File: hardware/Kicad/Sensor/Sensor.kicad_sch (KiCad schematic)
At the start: 9 parts

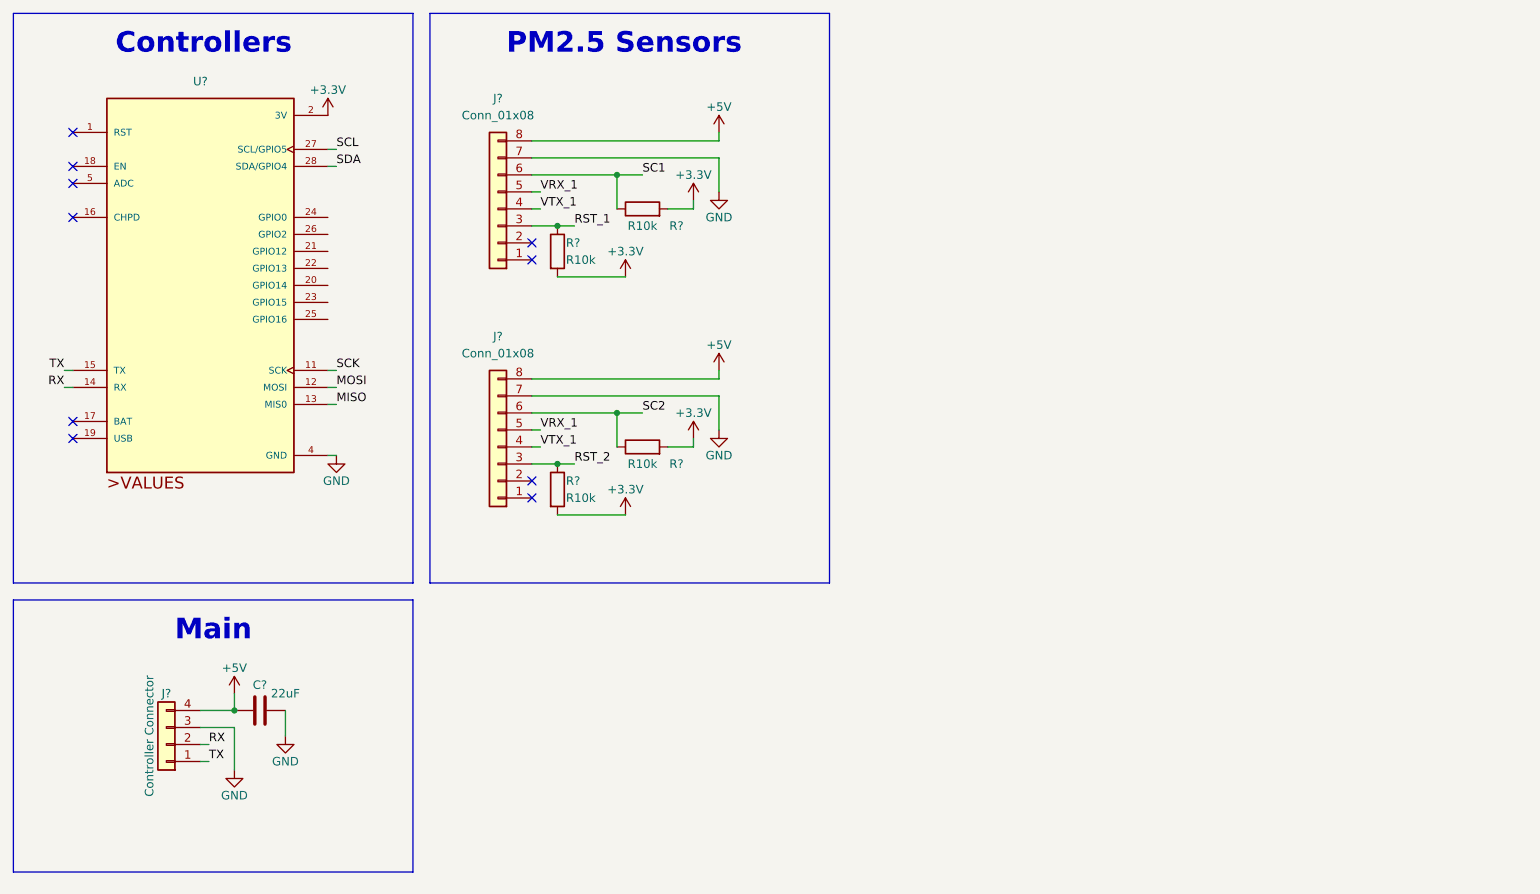
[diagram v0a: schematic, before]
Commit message: finished sensor PCB
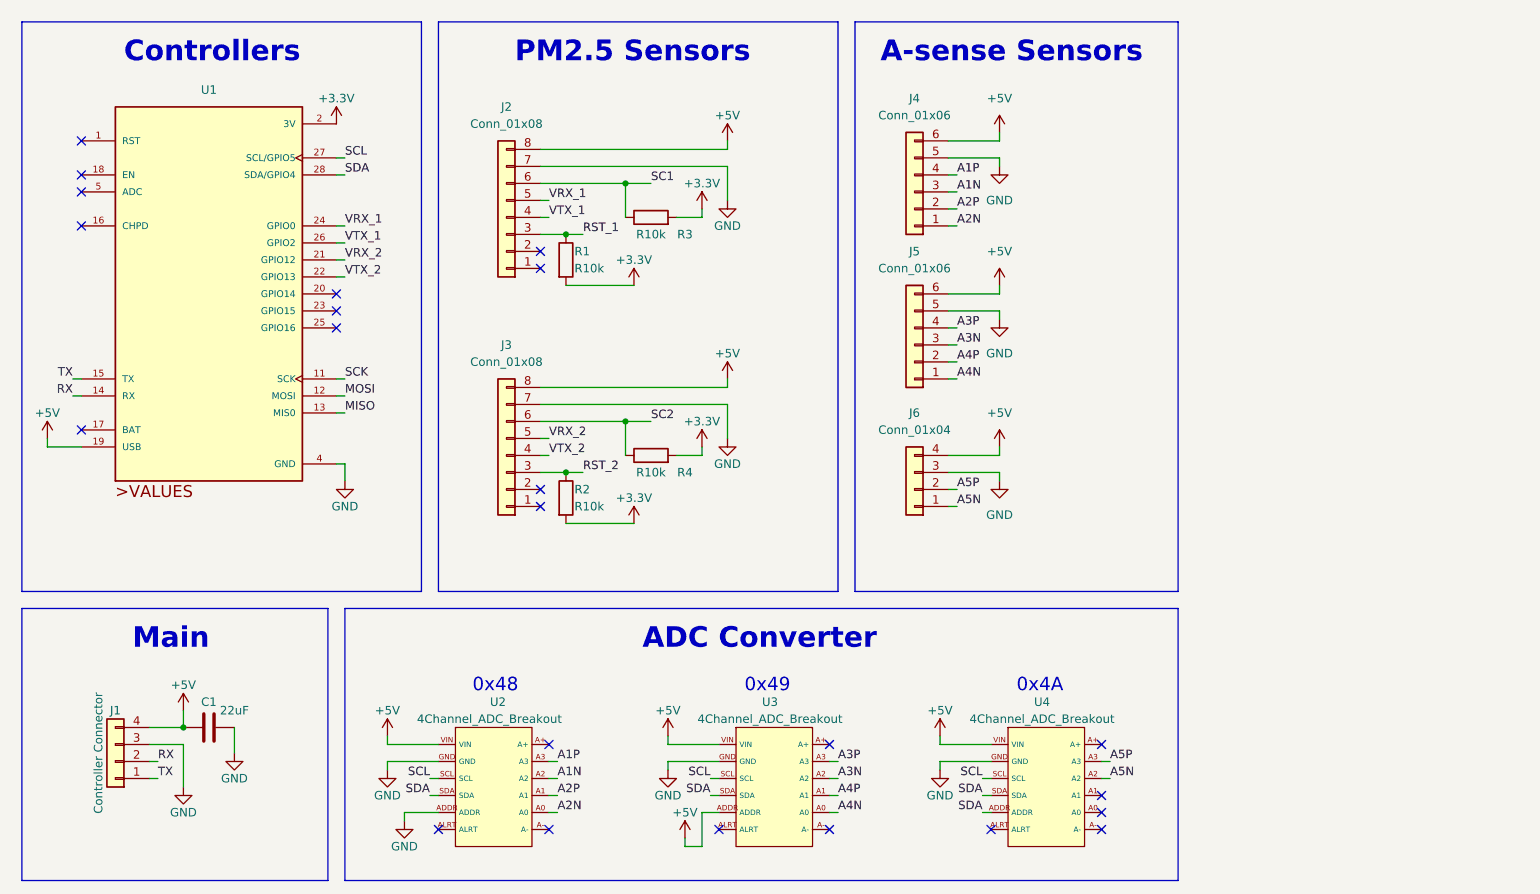
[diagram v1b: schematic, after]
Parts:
- added J4, J5: Conn_01x06, JST:JST_XH_B06B-XH-A_06x2.50mm_Straight, symbol Connector_Generic:Conn_01x06
- added J6: Conn_01x04, JST:JST_XH_B04B-XH-A_04x2.50mm_Straight, symbol Connector_Generic:Conn_01x04
- added U2, U3, U4: 4Channel_ADC_Breakout, Adafruit_Sensors:4Channel ADC Breakout, symbol Adafruit_Files:4Channel_ADC_Breakout
- J2, J3: renamed from J?; footprint (none) -> Connector_Molex:Molex_CLIK-Mate_502386-0870_1x08-1MP_P1.25mm_Horizontal
- R1, R2, R3, R4: renamed from R?; footprint (none) -> Resistor_SMD:R_1206_3216Metric
- gave numbers to parts that had none: 3
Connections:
- net +5V: now also U1.19 (USB), J4.6 (Pin_6), J5.6 (Pin_6), J6.4 (Pin_4), U2.VIN, U3.ADDR, U3.VIN, U4.VIN
- net GND: now also J4.5 (Pin_5), J5.5 (Pin_5), J6.3 (Pin_3), U2.ADDR, U2.GND, U3.GND, U4.GND
- net SCL: now also U2.SCL, U3.SCL, U4.SCL
- net SDA: now also U2.SDA, U3.SDA, U4.ADDR, U4.SDA
- net VRX_1: now also U1.24 (GPIO0); no longer J3.5 (Pin_5)
- net VTX_1: now also U1.26 (GPIO2); no longer J3.4 (Pin_4)
- net VRX_2: now reaches U1.21 (GPIO12)
- net VRX_2: now also J3.5 (Pin_5)
- net VTX_2: now reaches U1.22 (GPIO13)
- net VTX_2: now also J3.4 (Pin_4)
- new net A1N: J4.3 (Pin_3), U2.A2
- new net A1P: J4.4 (Pin_4), U2.A3
- new net A2N: J4.1 (Pin_1), U2.A0
- new net A2P: J4.2 (Pin_2), U2.A1
- new net A3N: J5.3 (Pin_3), U3.A2
- new net A3P: J5.4 (Pin_4), U3.A3
- new net A4N: J5.1 (Pin_1), U3.A0
- new net A4P: J5.2 (Pin_2), U3.A1
- new net A5N: J6.1 (Pin_1), U4.A2
- new net A5P: J6.2 (Pin_2), U4.A3
- no-connect marks 10 -> 23
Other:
- note added: "0x48"
- note added: "0x49"
- note added: "0x4A"
- note added: "A-sense Sensors"
- note added: "ADC Converter"
- moved on the sheet: C1, J1, J2, J3, R1, R2, R3, R4, U1

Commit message: updated PCBS
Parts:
- removed U4: 4Channel_ADC_Breakout, Adafruit_Sensors:4Channel ADC Breakout, symbol Adafruit_Files:4Channel_ADC_Breakout
- added U4: MicroSD_Breakout, Adafruit_Sensors:MicroSD_Breakout, symbol Adafruit_Files:MicroSD_Breakout
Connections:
- net A5N is gone; now on net A3P: J6.1 (Pin_1)
- net A5P is gone; now on net A3N: J6.2 (Pin_2)
- net +5V: now also U4.5V
- net A1N: now also J4.2 (Pin_2); no longer J4.3 (Pin_3)
- net A2N: now also J5.2 (Pin_2); no longer J4.1 (Pin_1)
- net A2P: now also J5.4 (Pin_4); no longer J4.2 (Pin_2)
- net A3N: no longer J5.3 (Pin_3)
- net A3P: no longer J5.4 (Pin_4)
- net GND: now also J4.1 (Pin_1), J4.3 (Pin_3), J5.1 (Pin_1), J5.3 (Pin_3), U4.GND
- net MISO: now also U4.DO
- net MOSI: now also U4.DI
- net SCK: now also U4.CLK
- net CS1: now reaches U1.20 (GPIO14)
- net CS1: now also U4.CS
- net A4N: no longer names the net of U3.A0
- net A4N: no longer J5.1 (Pin_1)
- net A4P: no longer names the net of U3.A1
- net A4P: no longer J5.2 (Pin_2)
- no-connect marks 23 -> 20
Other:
- note added: "Micro SD"
- note removed: "0x4A"
- moved on the sheet: J5, J6

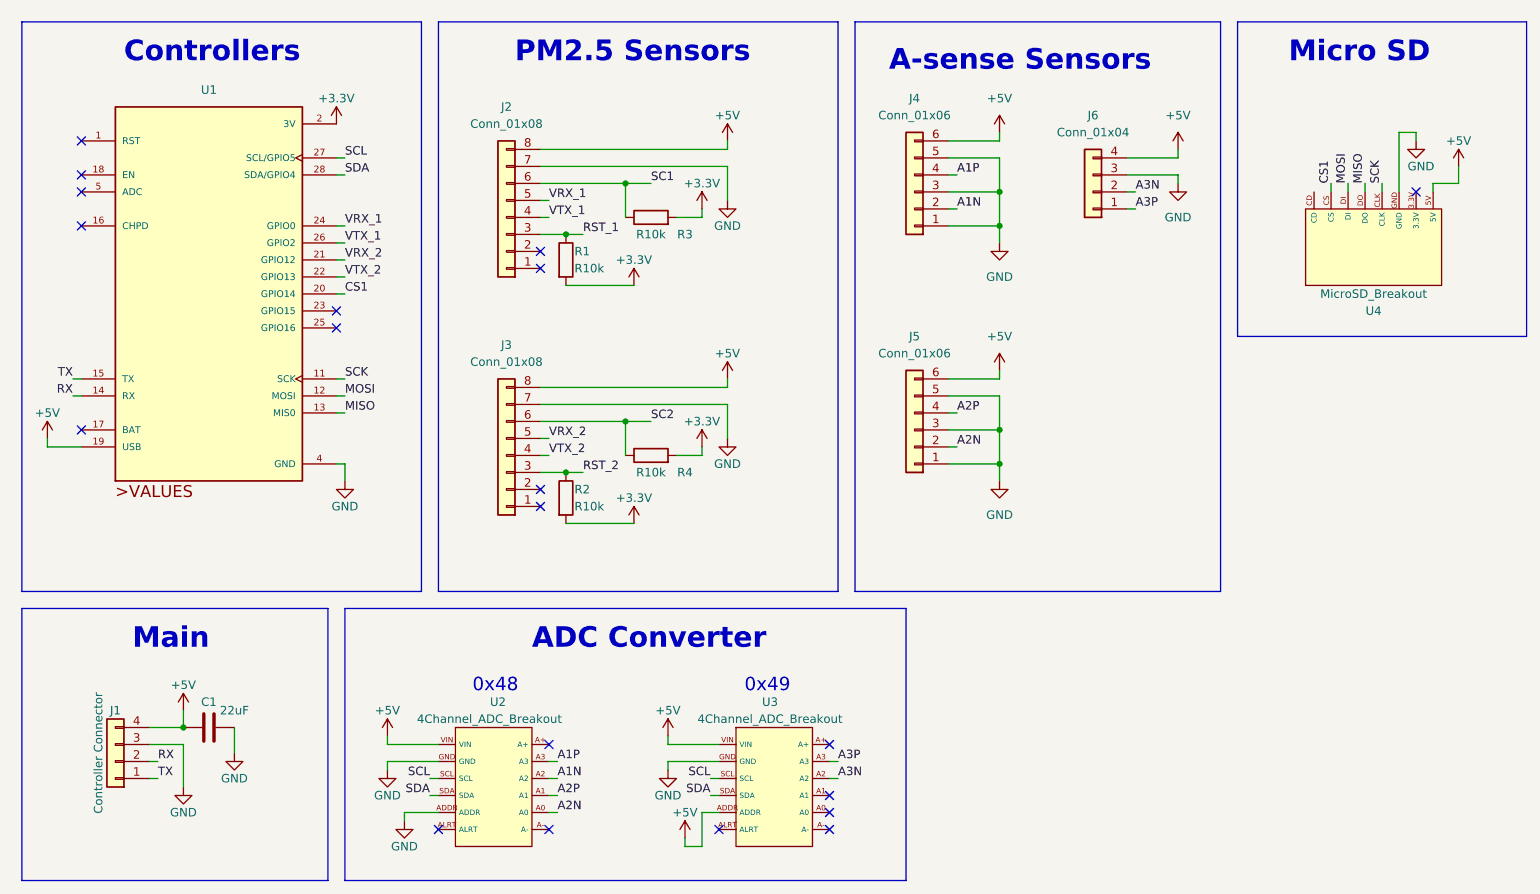
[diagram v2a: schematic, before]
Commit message: added extra resistor
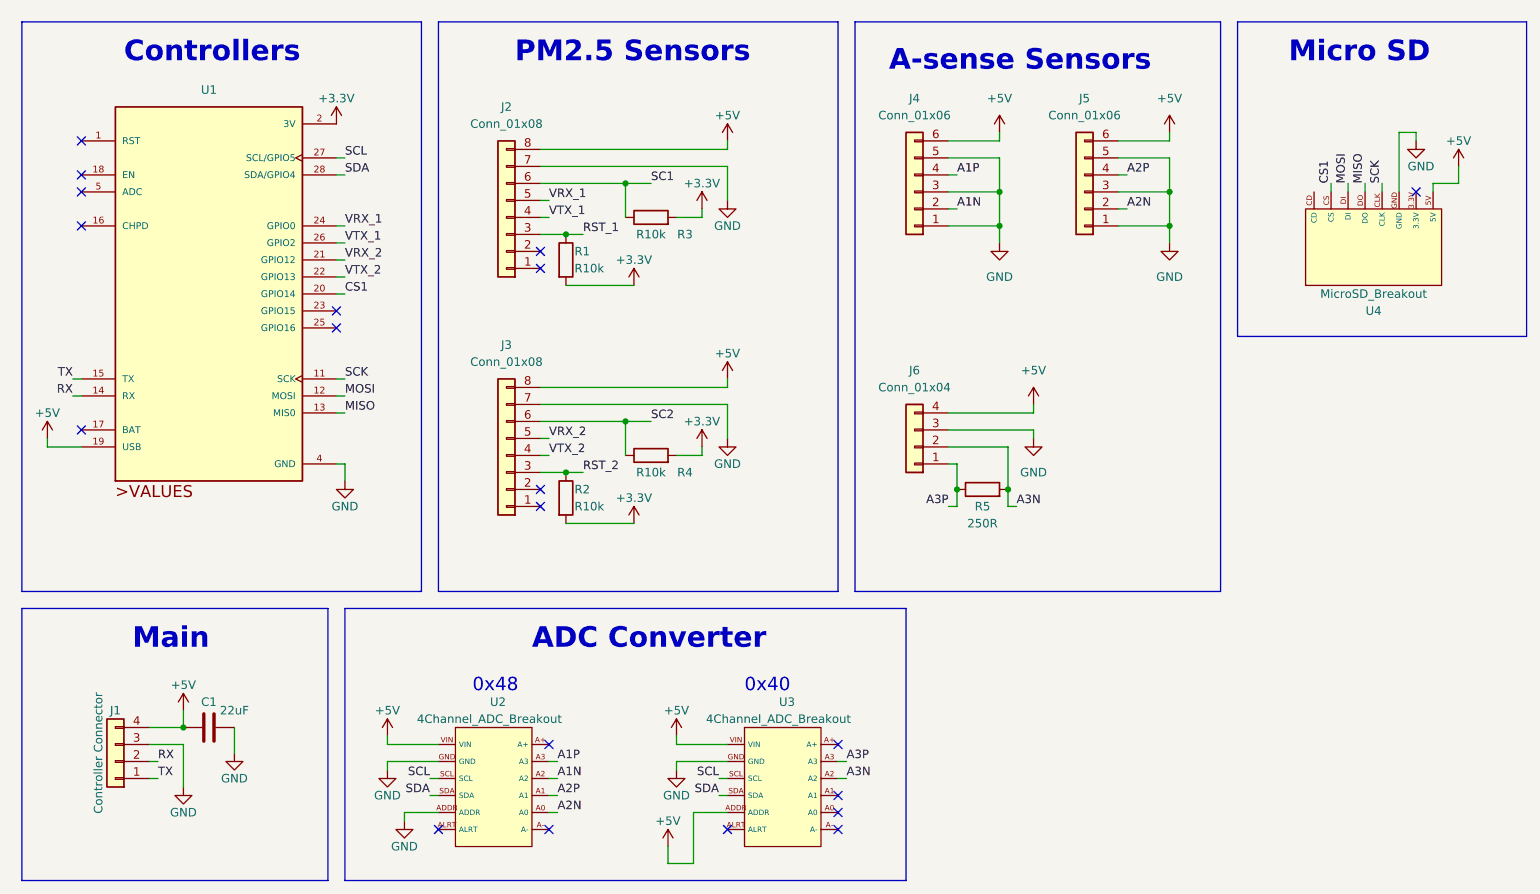
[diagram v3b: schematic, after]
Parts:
- added R5: 250R, Resistor_SMD:R_0805_2012Metric, symbol Device:R
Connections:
- net A3N: now also R5.2
- net A3P: now also R5.1
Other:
- note added: "0x40"
- note removed: "0x49"
- moved on the sheet: J5, J6
